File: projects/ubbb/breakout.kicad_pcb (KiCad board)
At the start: 2 copper layers, 40.6 x 17.8 mm, 16 parts, among them CON1 USB-MINI-B, IC1 AT90USB162-A, P1 CONN_2, P2 CONN_8, P3 CONN_8, P4 CONN_8, P5 CONN_8, P7 ISP, X1 CRYSTAL_RESONATOR

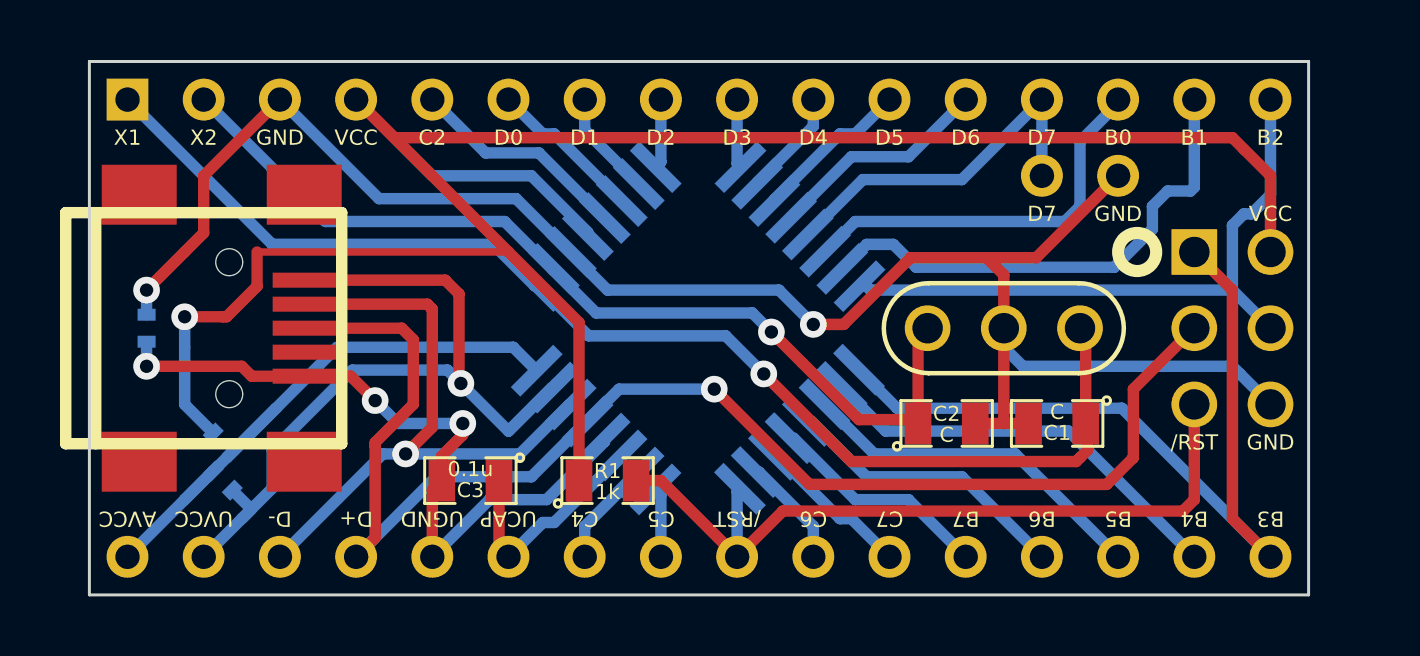
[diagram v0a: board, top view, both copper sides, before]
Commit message: moving breakout to ubbb
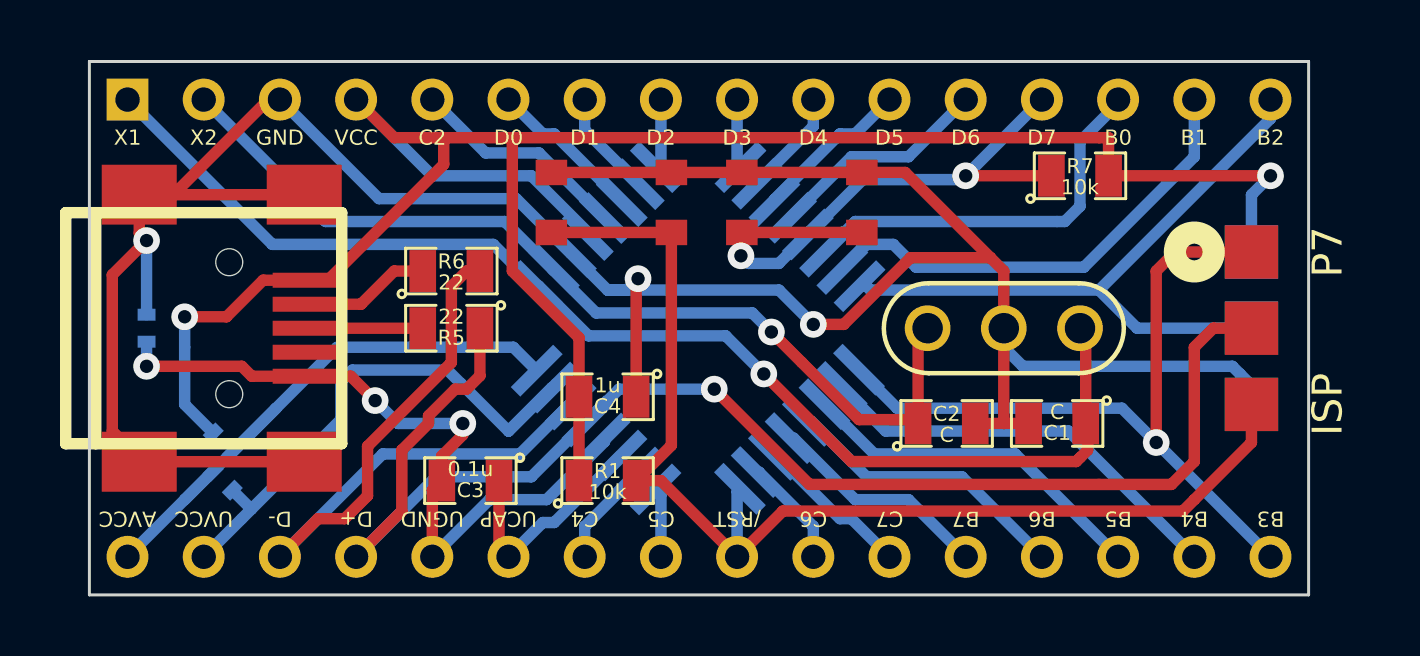
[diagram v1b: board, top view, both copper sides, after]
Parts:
- removed P1: CONN_2, conn:SIL-2
- added C4: 1u, cms:SM0805, F.Cu at (99.8, 106.4)
- added R5: 22, cms:SM0805, F.Cu at (94.6, 104.1)
- added R6: 22, cms:SM0805, F.Cu at (94.6, 102.2)
- added R7: 10k, cms:SM0805, F.Cu at (115.6, 99.1)
- added SW1: SW_PUSH_SMALL, custom:sw_42_32, F.Cu at (99.9, 99.9)
- added SW2: SW_PUSH_SMALL, custom:sw_42_32, F.Cu at (106.3, 99.9)
- P7: footprint custom:ISP -> custom:ISP_EDGE
- R1: value 1k -> 10k
- moved P7 3.17 mm to (123.8, 104.1), turned to 90 degrees
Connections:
- CON1 pad 1: /a31 -> /a4
- CON1 pad 2: /a30 -> Net-(CON1-Pad2)
- CON1 pad 3: /a29 -> Net-(CON1-Pad3)
- CON1 pad 6: Net-(CON1-Pad6) -> GND
- CON1 pad 7: Net-(CON1-Pad7) -> GND
- CON1 pad 8: Net-(CON1-Pad8) -> GND
- CON1 pad 9: Net-(CON1-Pad9) -> GND
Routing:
- net GND: track 60.0 -> 95.8 mm, vias 2 -> 3
- net /a24: track 25.9 -> 39.5 mm
- net /a31: track 28.2 -> 19.5 mm, vias 1 -> 0
- net /a13: track 12.2 -> 20.2 mm, vias 0 -> 2
- net Net-(CON1-Pad2): track 0.00 -> 4.31 mm
- net Net-(CON1-Pad3): track 0.00 -> 3.85 mm
- net /a30: track 21.3 -> 24.9 mm, vias 1 -> 0
- net /a4: track 76.1 -> 73.4 mm, vias 1 -> 2
- net /a17: track 27.5 -> 25.5 mm, vias 0 -> 1
- net /a16: track 21.3 -> 22.4 mm
- net /a15: track 16.9 -> 15.8 mm
- net /a29: track 46.8 -> 47.4 mm
